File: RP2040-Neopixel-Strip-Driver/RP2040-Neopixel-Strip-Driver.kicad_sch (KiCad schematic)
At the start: 0 parts

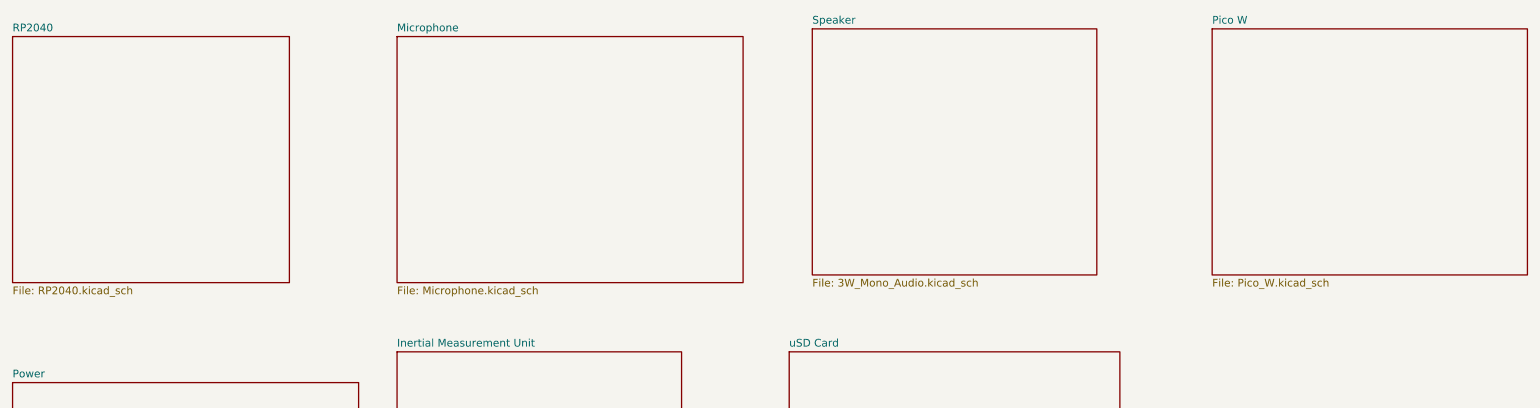
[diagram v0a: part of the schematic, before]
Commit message: Removed RP2040 Schematic, Going with Pico W Module
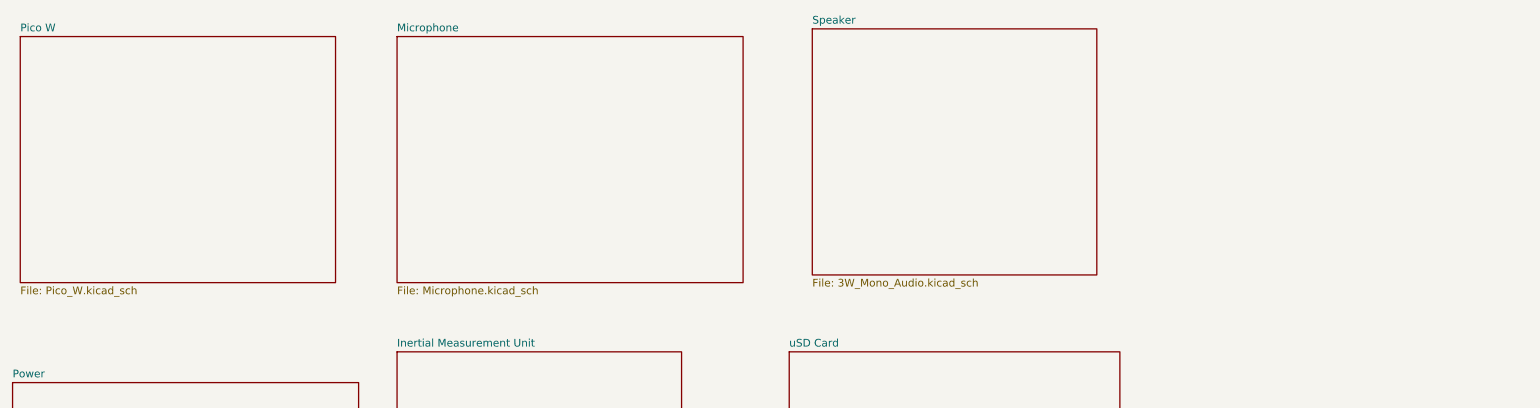
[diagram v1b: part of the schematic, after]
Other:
- removed sheet RP2040
